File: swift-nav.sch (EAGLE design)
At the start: 137 parts, among them J1 SMA_EDGE, J6 ZX62-B-5PA, U1 6SLX9FTG256, U10 MAX2769, U12 PT7M8206B33TA5EX, U13 M25PX80, U2 LTC3407A_DFN, U3 STM32-M-64-LQFP, U4 7Q-16.368MBG-T, U5 SMA_PATCH, U6 93LC56BT-I/OT, U7 FT232HQ, U8 B4050, X4 NX5032GA-12M, X5 CONN_5-2

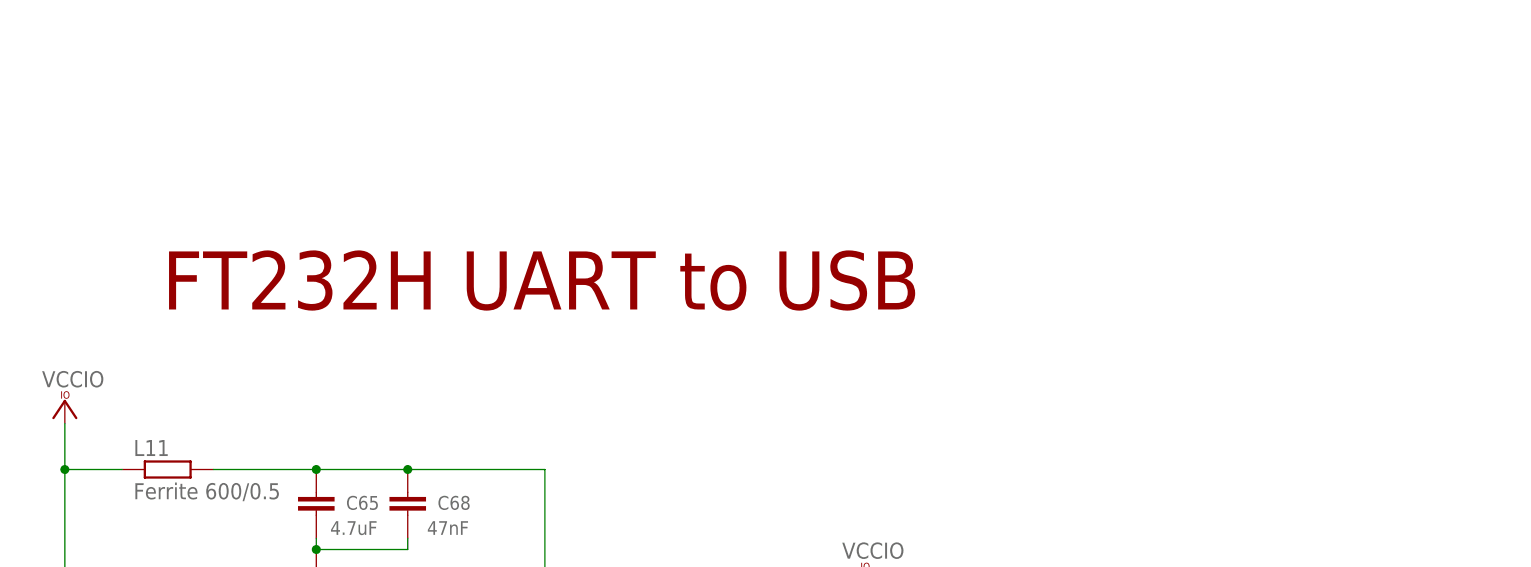
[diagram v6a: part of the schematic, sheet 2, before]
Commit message: All components placed inside can with 20 mil clearances for assembly
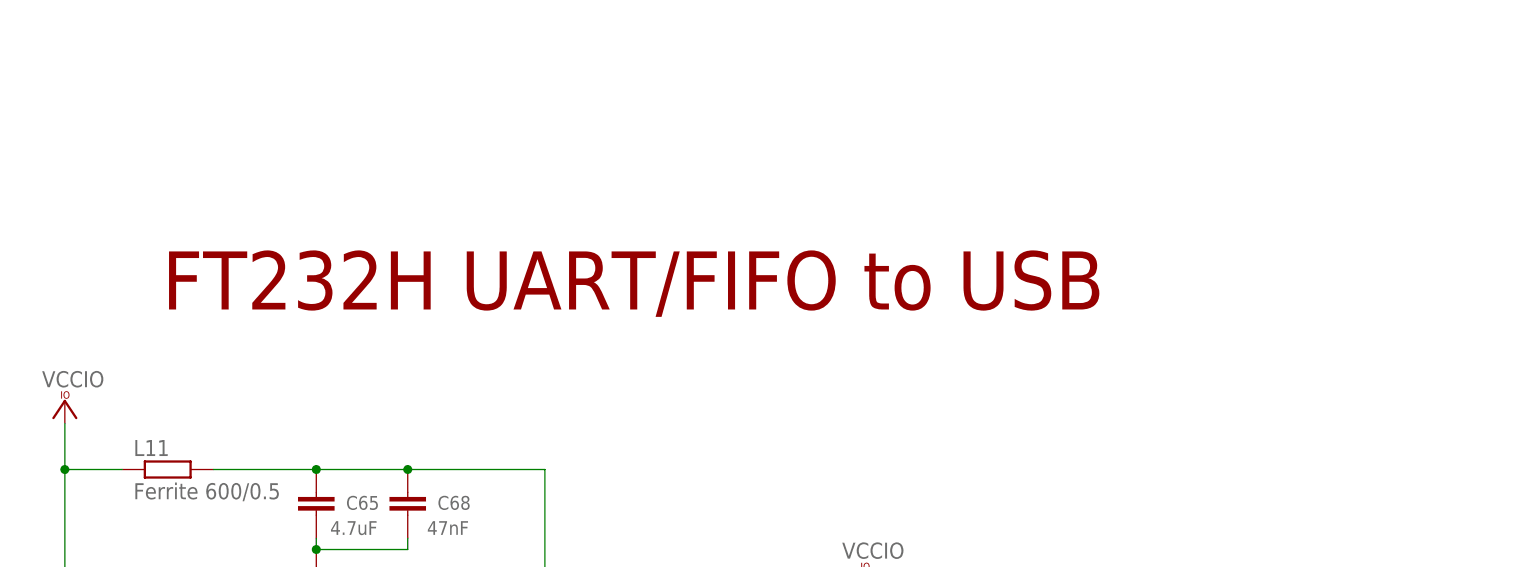
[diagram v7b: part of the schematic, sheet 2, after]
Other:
- note added: "FT232H UART/FIFO to USB"
- note removed: "FT232H UART to USB"
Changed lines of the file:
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@@
 <setting verticaltext="up"/>
 </settings>
-<grid distance="50" unitdist="mil" unit="mil" style="lines" multiple="1" display="yes" altdistance="0.01" altunitdist="inch" altunit="inch"/>
+<grid distance="0.1" unitdist="inch" unit="inch" style="lines" multiple="1" display="no" altdistance="0.01" altunitdist="inch" altunit="inch"/>
 <layers>
 <layer number="1" name="Top" color="4" fill="1" visible="no" active="no"/>
@@
 <text x="433.705" y="355.6" size="3.81" layer="97">Outer RF shield</text>
 <text x="158.75" y="308.61" size="2.54" layer="97">Reset Button</text>
-<text x="399.415" y="218.44" size="6.4516" layer="94">FT232H UART to USB</text>
+<text x="399.415" y="218.44" size="6.4516" layer="94">FT232H UART/FIFO to USB</text>
 <text x="535.94" y="101.6" size="1.778" layer="97">Change to 10k?</text>
 </plain>

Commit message: Just a bit of routing between the STM and FPGA left
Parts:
- added C100, C101, C102, C103, C104, C105, C106, C78, C80, C81, C83, C84, C85, C88, C89, C90, C91, C92, C93, C94, C95, C96, C97, C98, C99: 0.47uF, rcl:C-EUC0402
- added C46, C79: 4.7uF, rcl:C-EUC0603K
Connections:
- removed net 3: J1.3
- removed net 5: J1.5
- new net GND1: C103.2, C104.2, C105.2, C106.2
- net DEBUG0: no longer U1B3.IO_L32N_M3DQ15_3
- net DEBUG1: no longer U1B3.IO_L32P_M3DQ14_3
- net DEBUG2: no longer U1B3.IO_L33N_M3DQ13_3
- net DEBUG3: no longer U1B3.IO_L33P_M3DQ12_3
- net DEBUG4: no longer U1B3.IO_L34N_M3UDQSN_3
- net DEBUG5: no longer U1B3.IO_L34P_M3UDQS_3
- net DEBUG6: no longer U1B3.IO_L35N_M3DQ11_3
- net FTDI_ADBUS5: now also U1B3.IO_L52N_M3A9_3; no longer U1B3.IO_L47P_M3A0_3
- net FTDI_ADBUS6: now also U1B3.IO_L50N_M3BA2_3; no longer U1B3.IO_L48N_M3BA1_3
- net FTDI_ADBUS7: now also U1B3.IO_L50P_M3WE_3; no longer U1B3.IO_L48P_M3BA0_3
- net FTDI_CLKOUT: now also U1B3.IO_L41N_GCLK26_M3DQ5_3; no longer U1B3.IO_L44P_GCLK21_M3A5_3
- net FTDI_NTXE: now also U1B3.IO_L49N_M3A2_3; no longer U1B3.IO_L45N_M3ODT_3
- net FTDI_NWR: now also U1B3.IO_L46N_M3CLKN_3; no longer U1B3.IO_L45P_M3A3_3
- net GND: now also C100.2, C101.2, C102.2, C46.2, C78.2, C79.2, C80.2, C81.2, C83.2, C84.2, C85.2, C88.2, C89.2, C90.2, C91.2, C92.2, C93.2, C94.2, C95.2, C96.2, C97.2, C98.2, C99.2, J1.3, J1.5
- net MAX_CLKOUT: now also U1B3.IO_L40N_M3DQ7_3; no longer U1B0.IO_L37P_GCLK13_0
- net MAX_I0: now also U1B3.IO_L37N_M3DQ1_3; no longer U1B0.IO_L39N_0
- net MAX_I1: now also U1B3.IO_L36N_M3DQ9_3; no longer U1B0.IO_L39P_0
- net MAX_Q0: now also U1B3.IO_L38N_M3DQ3_3; no longer U1B0.IO_L38N_VREF_0
- net MAX_Q1: now also U1B3.IO_L39N_M3LDQSN_3; no longer U1B0.IO_L38P_0
- net SPI1MISO: no longer U1B3.IO_L40N_M3DQ7_3
- net SPI1MOSI: no longer U1B3.IO_L39P_M3LDQS_3
- net SPI1NSS: no longer U1B3.IO_L40P_M3DQ6_3
- net SPI1SCK: no longer U1B3.IO_L41N_GCLK26_M3DQ5_3
- net STM_CLK_IN: no longer U1B3.IO_L50N_M3BA2_3
- net V+: now also C96.1
- net VCC: now also C91.1, C92.1, C93.1, C94.1
- net VCCINT: now also C46.1, C78.1, C79.1, C80.1
- net VCCIO: now also C100.1, C101.1, C102.1, C103.1, C104.1, C105.1, C106.1, C81.1, C83.1, C84.1, C85.1, C88.1, C89.1, C90.1, C95.1, C97.1, C98.1, C99.1
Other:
- note added: "Bypass Caps for Patch Balance"
- note added: "Spartan Bypass Patch Side - VCCINT"
- note added: "Spartan Patch Side Optional Bypass - VCCIO"
- moved on the sheet: X3
